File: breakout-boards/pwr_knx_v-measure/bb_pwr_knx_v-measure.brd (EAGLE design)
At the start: 28.5 x 25 mm, 47 parts, among them IC100 BD9G101, T1 BC856, T2 BCP52, T3 BC847

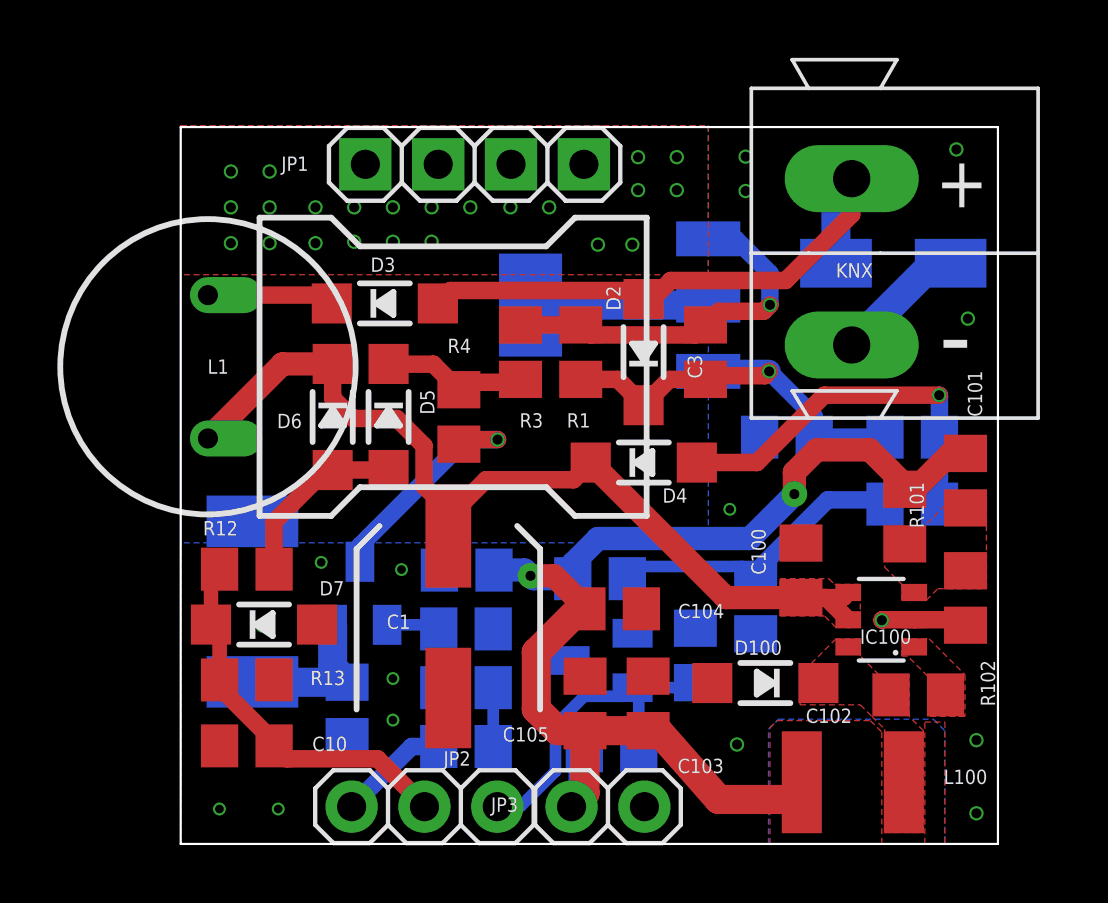
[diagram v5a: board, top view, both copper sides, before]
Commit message: [BB_Pwr+KNX] - widened holes for power inductor
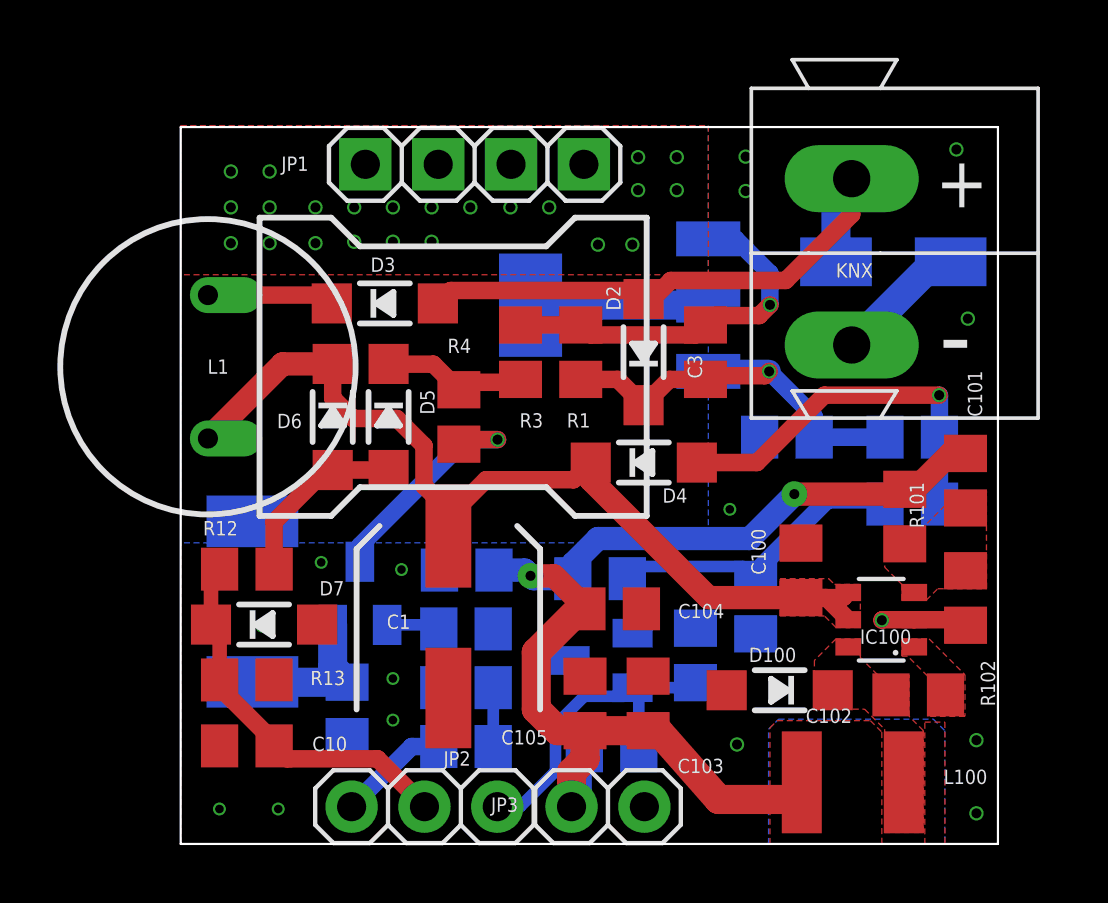
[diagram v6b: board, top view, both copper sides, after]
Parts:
- moved D100 0.56 mm to (22.4, 5.36)
- moved D1 0.05 mm to (26.4, 20.3)
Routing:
- net +3V3: track 43.2 -> 41.5 mm
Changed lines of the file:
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@@
 <attribute name="VALUE" x="28.241" y="14.00275" size="0.5" layer="27" rot="R270"/>
 </element>
-<element name="D100" library="microbuilder" package="SOD-123" value="MBRS1100" x="21.8887" y="5.61" smashed="yes" rot="R180">
-<attribute name="NAME" x="21.638690625" y="7.09399375" size="0.5" layer="25" rot="R180" align="bottom-center"/>
-<attribute name="VALUE" x="18.938696875" y="4.52599375" size="0.5" layer="27" rot="R180" align="top-center"/>
+<element name="D100" library="microbuilder" package="SOD-123" value="MBRS1100" x="22.3887" y="5.36" smashed="yes" rot="R180">
+<attribute name="NAME" x="22.138690625" y="6.84399375" size="0.5" layer="25" rot="R180" align="bottom-center"/>
+<attribute name="VALUE" x="19.438696875" y="4.27599375" size="0.5" layer="27" rot="R180" align="top-center"/>
 </element>
 <element name="R9" library="rcl" library_urn="urn:adsk.eagle:library:334" package="R0805" package3d_urn="urn:adsk.eagle:package:23553/2" value="100k" x="21.55" y="8.275" smashed="yes" rot="MR90">
@@
 <attribute name="VALUE" x="4.4882" y="4.379" size="0.5" layer="27"/>
 </element>
-<element name="D1" library="smaj_10" package="DO214AC" value="SMAJ40CA" x="26.35" y="20.25" smashed="yes" rot="MR180">
-<attribute name="MF" value="Littelfuse" x="26.35" y="20.25" size="1.016" layer="28" rot="MR180" display="off"/>
-<attribute name="MPN" value="SMAJ40CA" x="26.35" y="20.25" size="1.016" layer="28" rot="MR180" display="off"/>
-<attribute name="NAME" x="29.1" y="22.05" size="0.5" layer="26" rot="MR0"/>
-<attribute name="OC_FARNELL" value="1827675" x="26.35" y="20.25" size="1.016" layer="28" rot="MR180" display="off"/>
-<attribute name="OC_NEWARK" value="71J2019" x="26.35" y="20.25" size="1.016" layer="28" rot="MR180" display="off"/>
-<attribute name="VALUE" x="24.15" y="20.4" size="0.5" layer="28" rot="MR180"/>
+<element name="D1" library="smaj_10" package="DO214AC" value="SMAJ40CA" x="26.35" y="20.3" smashed="yes" rot="MR180">
+<attribute name="MF" value="Littelfuse" x="26.35" y="20.3" size="1.016" layer="28" rot="MR180" display="off"/>
+<attribute name="MPN" value="SMAJ40CA" x="26.35" y="20.3" size="1.016" layer="28" rot="MR180" display="off"/>
+<attribute name="NAME" x="29.1" y="22.1" size="0.5" layer="26" rot="MR0"/>
+<attribute name="OC_FARNELL" value="1827675" x="26.35" y="20.3" size="1.016" layer="28" rot="MR180" display="off"/>
+<attribute name="OC_NEWARK" value="71J2019" x="26.35" y="20.3" size="1.016" layer="28" rot="MR180" display="off"/>
+<attribute name="VALUE" x="24.15" y="20.45" size="0.5" layer="28" rot="MR180"/>
 </element>
 <element name="D3" library="microbuilder" package="SOD-123" value="1N4148" x="8.619" y="18.85" smashed="yes">
@@
 </element>
 <element name="C105" library="rcl" library_urn="urn:adsk.eagle:library:334" package="C0805" package3d_urn="urn:adsk.eagle:package:23617/2" value="47uF 10V" x="15.6" y="4.9" smashed="yes" rot="R90">
-<attribute name="NAME" x="12.73" y="3.57" size="0.5" layer="25"/>
+<attribute name="NAME" x="12.68" y="3.47" size="0.5" layer="25"/>
 <attribute name="POPULARITY" value="88" x="15.6" y="4.9" size="1.778" layer="27" rot="R90" display="off"/>
 <attribute name="SPICEPREFIX" value="C" x="15.6" y="4.9" size="1.778" layer="27" rot="R90" display="off"/>
@@
 <via x="21.2" y="22.76875" extent="1-16" drill="0.35"/>
 <via x="4.35" y="7.61875" extent="1-16" drill="0.35"/>
-<wire x1="28.35" y1="20.25" x2="27.75" y2="20.25" width="1.016" layer="16"/>
-<wire x1="24.9" y1="17.4" x2="27.75" y2="20.25" width="1.016" layer="16"/>
+<wire x1="28.35" y1="20.3" x2="27.8" y2="20.3" width="1.016" layer="16"/>
+<wire x1="24.9" y1="17.4" x2="27.8" y2="20.3" width="1.016" layer="16"/>
 <via x="6.4" y="9.81875" extent="1-16" drill="0.3"/>
 <via x="9.2" y="9.56875" extent="1-16" drill="0.3"/>
@@
 <polygon width="0.0762" layer="1" thermals="no">
 <vertex x="24.35" y="7.15"/>
-<vertex x="23.25" y="6.05"/>
-<vertex x="23.1" y="6.05"/>
-<vertex x="23.1" y="4.85"/>
-<vertex x="25.2" y="4.85"/>
-<vertex x="25.6" y="4.45"/>
+<vertex x="23.6" y="6.4"/>
+<vertex x="23.6" y="4.7"/>
+<vertex x="25.35" y="4.7"/>
 <vertex x="26.05" y="4"/>
-<vertex x="26.05" y="3.9"/>
 <vertex x="26.05" y="0.4"/>
 <vertex x="27.4" y="0.4"/>
@@
 <vertex x="26.9" y="4.45"/>
 <vertex x="26.9" y="5.9"/>
-<vertex x="25.85" y="5.9"/>
-<vertex x="25.2" y="6.55"/>
+<vertex x="25.8" y="5.9"/>
+<vertex x="25.2" y="6.5"/>
 <vertex x="25.2" y="7.15"/>
 </polygon>
@@
 <wire x1="24.9" y1="21.95" x2="22.6" y2="19.65" width="0.6096" layer="1"/>
 <wire x1="24.9" y1="23.2" x2="24.35" y2="23.2" width="1.016" layer="16"/>
-<wire x1="24.35" y1="23.2" x2="24.35" y2="20.25" width="1.016" layer="16"/>
+<wire x1="24.35" y1="23.2" x2="24.35" y2="20.3" width="1.016" layer="16"/>
 </signal>
 <signal name="N$6">
@@
 <wire x1="19.45" y1="17.75" x2="15.8" y2="17.75" width="0.6096" layer="1"/>
 <wire x1="15.8" y1="17.75" x2="15.45" y2="18.1" width="0.6096" layer="1"/>
-<wire x1="22.05" y1="18.8" x2="21.825" y2="18.575" width="0.6096" layer="1"/>
-<wire x1="21.825" y1="18.575" x2="20.275" y2="18.575" width="0.6096" layer="1"/>
-<wire x1="20.275" y1="18.575" x2="19.8" y2="18.1" width="0.6096" layer="1"/>
+<wire x1="22.05" y1="18.8" x2="21.675" y2="18.425" width="0.6096" layer="1"/>
+<wire x1="21.675" y1="18.425" x2="20.125" y2="18.425" width="0.6096" layer="1"/>
+<wire x1="20.125" y1="18.425" x2="19.8" y2="18.1" width="0.6096" layer="1"/>
 <via x="22.05" y="18.8" extent="1-16" drill="0.35"/>
 <wire x1="22.05" y1="18.8" x2="22.05" y2="19.9" width="0.6096" layer="16"/>
@@
 <vertex x="22.4" y="7.95"/>
 </polygon>
-<wire x1="23.13" y1="8.591" x2="20.509" y2="8.591" width="0.8128" layer="1"/>
-<wire x1="20.509" y1="8.591" x2="15.8" y2="13.3" width="0.8128" layer="1"/>
+<wire x1="23.13" y1="8.591" x2="19.909" y2="8.591" width="0.8128" layer="1"/>
+<wire x1="19.909" y1="8.591" x2="15.8" y2="12.7" width="0.8128" layer="1"/>
+<wire x1="15.8" y1="12.7" x2="15.8" y2="13.3" width="0.8128" layer="1"/>
 </signal>
 <signal name="+3V3">
@@
 <contactref element="L100" pad="2"/>
 <contactref element="JP3" pad="1"/>
-<wire x1="26.769" y1="12.36725" x2="26.75" y2="12.36725" width="0.8128" layer="1"/>
 <wire x1="23.1607" y1="1.9" x2="23.1607" y2="2.15" width="1.016" layer="1"/>
 <wire x1="23.1607" y1="1.9" x2="22.8107" y2="1.55" width="1.016" layer="1"/>
@@
 <wire x1="22.9" y1="12.2" x2="21.35" y2="10.65" width="0.8128" layer="16"/>
 <via x="22.9" y="12.2" extent="1-16" drill="0.35" diameter="0.9"/>
-<wire x1="22.9" y1="12.2" x2="22.9" y2="12.9600875" width="0.8128" layer="1"/>
 <wire x1="16.05" y1="10.65" x2="21.35" y2="10.65" width="0.8128" layer="16"/>
-<wire x1="22.9" y1="12.9600875" x2="23.6814625" y2="13.74155" width="0.8128" layer="1"/>
-<wire x1="25.5314625" y1="13.74155" x2="26.769" y2="12.5040125" width="0.8128" layer="1"/>
-<wire x1="26.769" y1="12.5040125" x2="26.769" y2="12.36725" width="0.8128" layer="1"/>
+<wire x1="26.4571625" y1="12.36725" x2="26.2899125" y2="12.2" width="0.8128" layer="1"/>
+<wire x1="22.9" y1="12.2" x2="26.2899125" y2="12.2" width="0.8128" layer="1"/>
 <wire x1="28.35" y1="13.61725" x2="27.1" y2="12.36725" width="0.8128" layer="1"/>
 <wire x1="26.75" y1="12.36725" x2="27.1" y2="12.36725" width="0.8128" layer="1"/>
 <wire x1="28.35" y1="13.61725" x2="28.869" y2="13.61725" width="0.8128" layer="1"/>
-<wire x1="23.6814625" y1="13.74155" x2="25.5314625" y2="13.74155" width="0.8128" layer="1"/>
+<wire x1="26.4571625" y1="12.36725" x2="26.75" y2="12.36725" width="0.8128" layer="1"/>
 <wire x1="15.575" y1="3.25" x2="15.43" y2="3.105" width="0.8128" layer="16"/>
 <wire x1="15.43" y1="3.105" x2="15.43" y2="1.66" width="0.8128" layer="16"/>
@@
 <wire x1="15.6" y1="3.95" x2="14.65" y2="3.95" width="1.016" layer="1"/>
 <wire x1="14.65" y1="3.95" x2="13.9" y2="4.7" width="1.016" layer="1"/>
-<wire x1="15.13" y1="1.3" x2="15.6" y2="1.77" width="1.016" layer="1"/>
-<wire x1="15.6" y1="1.77" x2="15.6" y2="3.95" width="1.016" layer="1"/>
+<wire x1="15.6" y1="2.97" x2="15.13" y2="2.5" width="1.016" layer="1"/>
+<wire x1="15.13" y1="1.3" x2="15.13" y2="2.5" width="1.016" layer="1"/>
+<wire x1="15.6" y1="2.97" x2="15.6" y2="3.95" width="1.016" layer="1"/>
 <wire x1="13.9" y1="4.7" x2="13.9" y2="6.684" width="1.016" layer="1"/>
 <wire x1="15.416" y1="8.2" x2="15.666" y2="8.2" width="1.016" layer="1"/>

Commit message: [BB_Pwr+KNX] - rearranged parts, reduced heat dissipation pins to 2
rearrangement in order to avoid by accident wrongly placed parts and connected pin headers
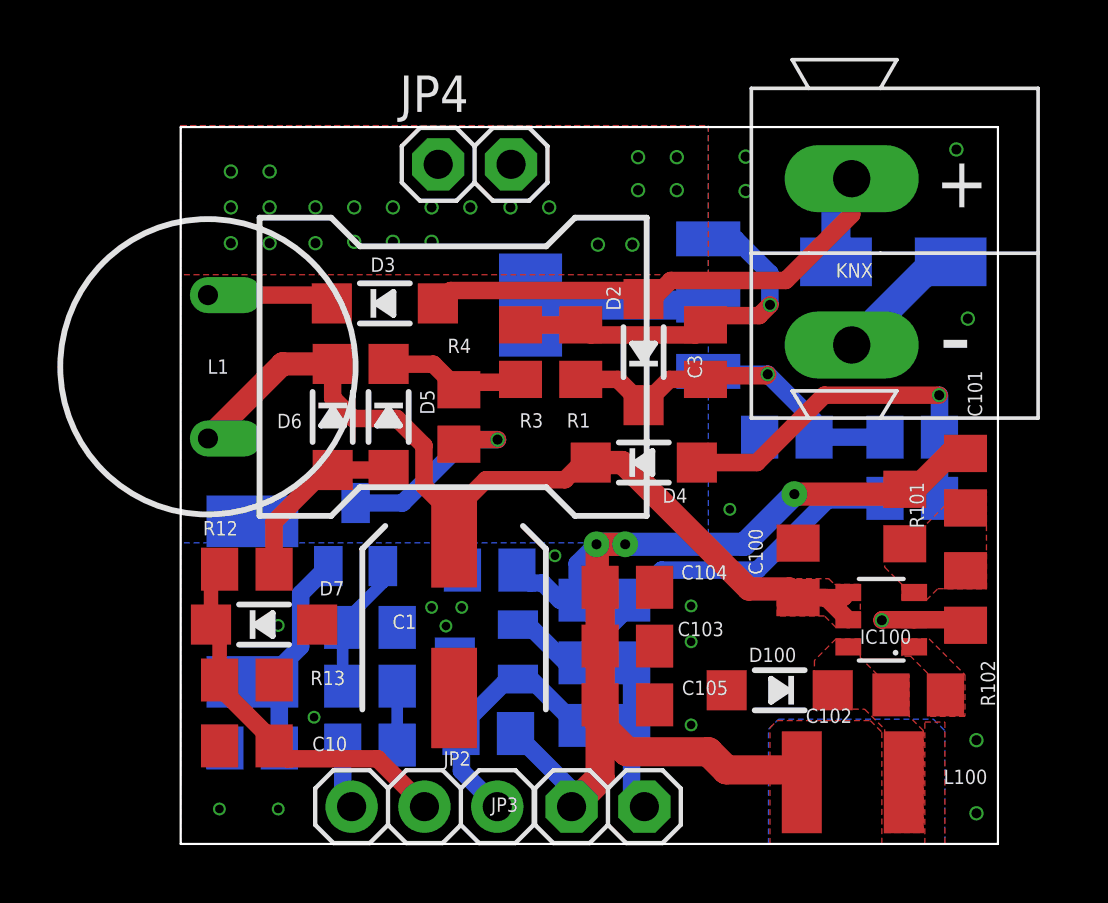
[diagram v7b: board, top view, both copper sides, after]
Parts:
- removed JP1: (no value), pinhead_dmx:1X04
- added JP4: (no value), pinhead_dmx:1X02
- moved R9 5.63 mm to (16.3, 6.32), turned to 0 degrees
- moved R7 4.34 mm to (12.2, 3.85), turned to 180 degrees
- moved T1 4.01 mm to (12.2, 6.70)
- moved C5 4.01 mm to (16.3, 4.13), turned to 0 degrees
- moved R2 3.57 mm to (3.99, 3.35), turned to 180 degrees
- moved C4 3.35 mm to (8.10, 3.45)
- moved R5 3.35 mm to (8.10, 7.55)
- moved R6 3.35 mm to (8.10, 5.50)
- moved C103 2.13 mm to (17.1, 6.90), turned to 0 degrees
- moved T3 2.06 mm to (7.60, 10.8)
- moved C105 1.48 mm to (17.1, 4.85), turned to 0 degrees
- moved C104 0.88 mm to (17.1, 8.95)
- moved C6 0.80 mm to (12.3, 9.55)
- moved R8 0.76 mm to (16.3, 8.50)
- moved C1 0.20 mm to (11.0, 7.89)
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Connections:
- net N$8: now also JP4.1, JP4.2; no longer JP1.1, JP1.2, JP1.3, JP1.4
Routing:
- net GND: track 7.66 -> 12.9 mm, vias 16 -> 19
- net EIB_IN: track 11.9 -> 8.77 mm
- net N$14: track 12.8 -> 15.9 mm
- net N$7: track 5.52 -> 7.91 mm
- net EIB_OUT: track 3.91 -> 2.28 mm
- net N$6: track 8.31 -> 7.28 mm
- net N$12: track 3.91 -> 4.77 mm
- net +3V3: vias 2 -> 3
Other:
- board text added: "Selfbus Power and KNX-Connection Board v0.9.2"
- board text removed: "Selfbus Power and KNX-Connection Board v0.9.1"

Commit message: [BB_Pwr+KNX] - labels rearranged; MLCC values updated
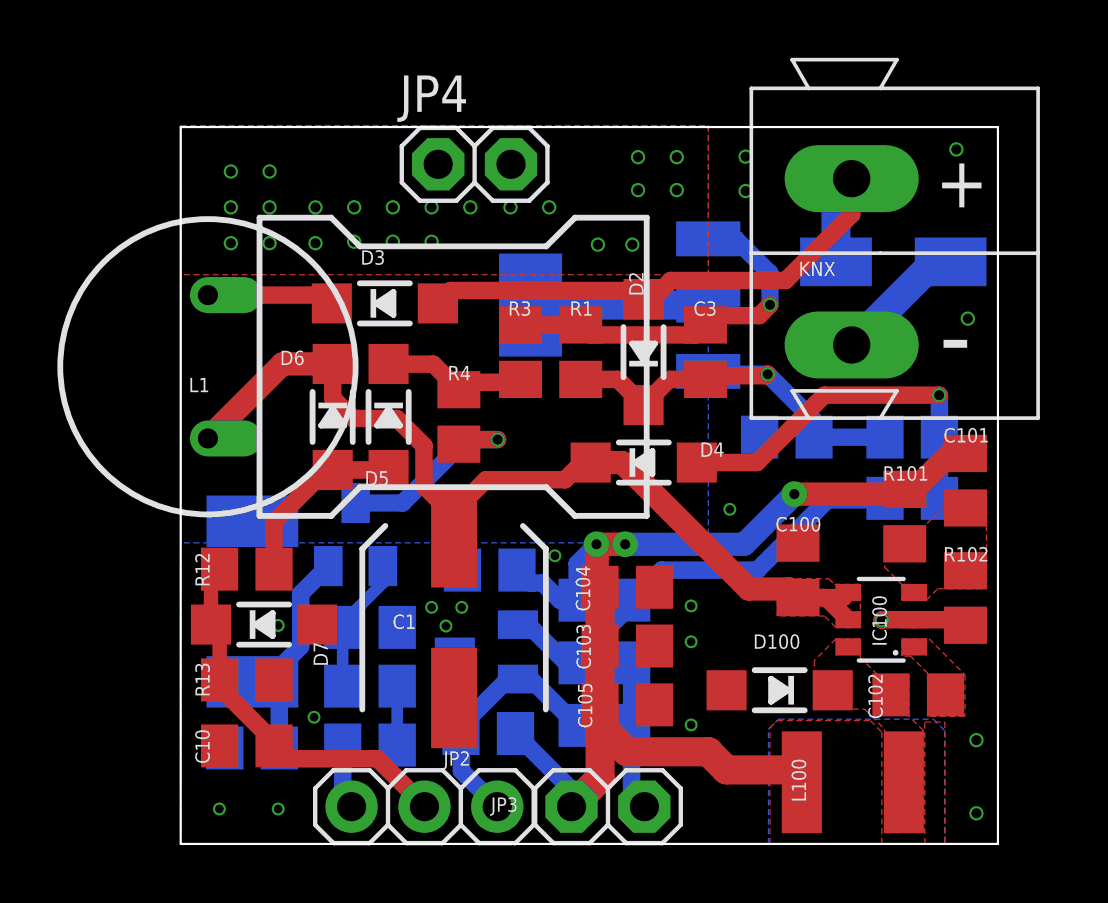
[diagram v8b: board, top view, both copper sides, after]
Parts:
- C10, C2, C6: value 100n -> 100nF
- C3, C4: value 10n -> 10nF
- C5: value 100p -> 100pF
